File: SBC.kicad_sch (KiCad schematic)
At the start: 0 parts

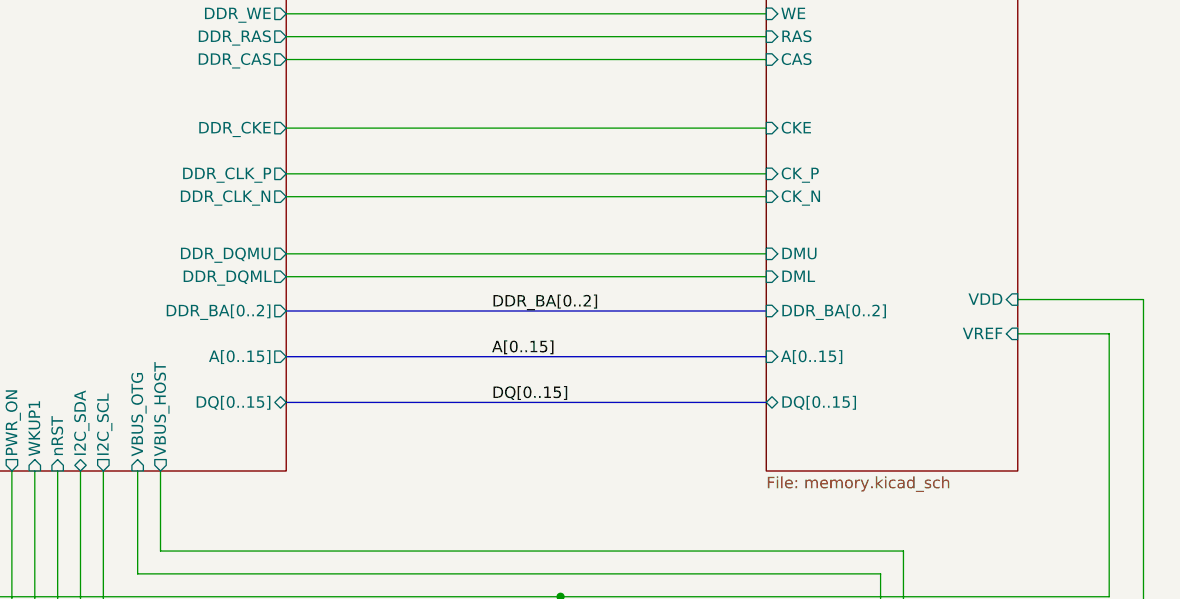
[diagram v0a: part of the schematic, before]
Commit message: DDR routing first pass complete
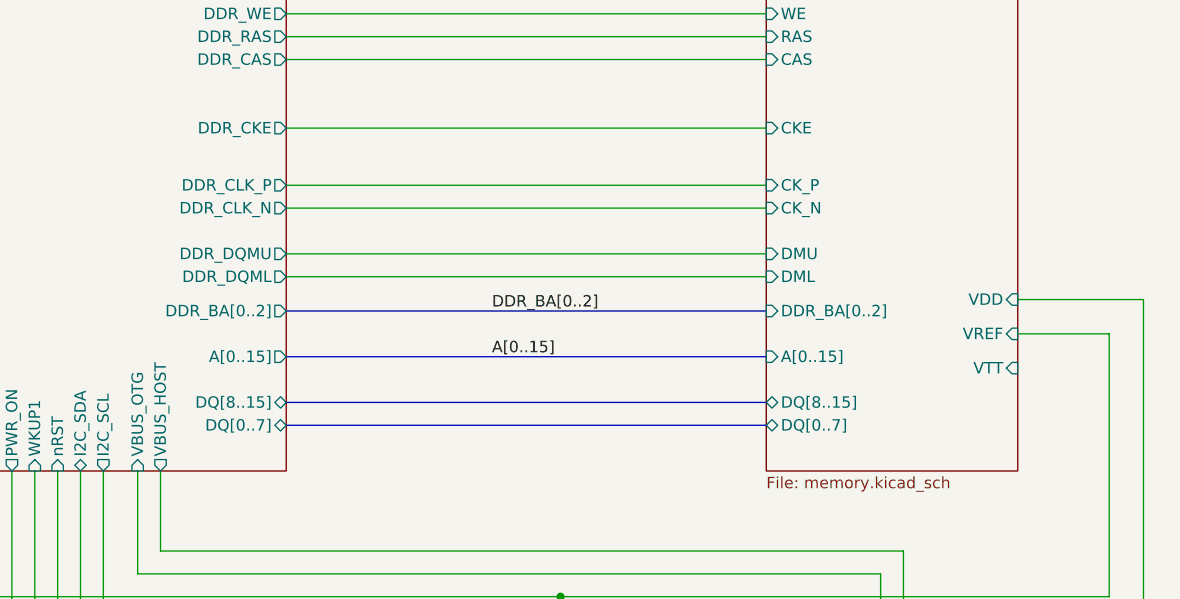
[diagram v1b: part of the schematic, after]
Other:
- sheet MPU ports: added DQ[0..7], DQ[8..15]; removed DQ[0..15]
- sheet Memory ports: added DQ[0..7], DQ[8..15], VTT; removed DQ[0..15]

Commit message: Routing routing routing
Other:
- sheet MPU ports: added SDMMC2_RESET, SDMMC2_STROBE; removed none
- sheet NAND ports: added DS; removed none
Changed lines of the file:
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@@
+	(wire
+		(pts
+			(xy 161.29 118.11) (xy 161.29 107.95)
+		)
+		(stroke
+			(width 0)
+			(type default)
+		)
+	)
 	(wire
 		(pts
@@
 	(wire
 		(pts
-			(xy 166.37 177.8) (xy 166.37 113.03)
+			(xy 168.91 177.8) (xy 168.91 115.57)
 		)
 		(stroke
@@
 	(wire
 		(pts
+			(xy 163.83 120.65) (xy 163.83 110.49)
+		)
+		(stroke
+			(width 0)
+			(type default)
+		)
+	)
+	(wire
+		(pts
 			(xy 205.74 142.24) (xy 205.74 205.74)
 		)
@@
 	(wire
 		(pts
+			(xy 161.29 107.95) (xy 179.07 107.95)
+		)
+		(stroke
+			(width 0)
+			(type default)
+		)
+	)
+	(wire
+		(pts
 			(xy 259.08 166.37) (xy 259.08 156.21)
 		)
@@
 	(wire
 		(pts
+			(xy 163.83 110.49) (xy 179.07 110.49)
+		)
+		(stroke
+			(width 0)
+			(type default)
+		)
+	)
+	(wire
+		(pts
 			(xy 214.63 142.24) (xy 214.63 151.13)
 		)
@@
 	(wire
 		(pts
+			(xy 147.32 118.11) (xy 161.29 118.11)
+		)
+		(stroke
+			(width 0)
+			(type default)
+		)
+	)
+	(wire
+		(pts
 			(xy 320.04 127) (xy 309.88 127)
 		)
@@
 	(wire
 		(pts
+			(xy 147.32 120.65) (xy 163.83 120.65)
+		)
+		(stroke
+			(width 0)
+			(type default)
+		)
+	)
+	(wire
+		(pts
 			(xy 228.6 74.93) (xy 281.94 74.93)
 		)
@@
 	(wire
 		(pts
-			(xy 166.37 113.03) (xy 179.07 113.03)
+			(xy 168.91 115.57) (xy 179.07 115.57)
 		)
 		(stroke
@@
 	(wire
 		(pts
-			(xy 234.95 177.8) (xy 166.37 177.8)
+			(xy 234.95 177.8) (xy 168.91 177.8)
 		)
 		(stroke
@@
 				(justify left bottom)
 				(hide yes)
+			)
+		)
+	)
+	(netclass_flag ""
+		(length 0.0254)
+		(shape round)
+		(at 154.94 100.33 0)
+		(effects
+			(font
+				(size 1.27 1.27)
+			)
+			(justify left bottom)
+		)
+		(property "Netclass" "EMMC"
+			(at 155.5496 100.3046 0)
+			(effects
+				(font
+					(size 1.27 1.27)
+					(italic yes)
+				)
+				(justify left bottom)
+			)
+		)
+	)
+	(netclass_flag ""
+		(length 0.0254)
+		(shape round)
+		(at 160.02 105.41 0)
+		(effects
+			(font
+				(size 1.27 1.27)
+			)
+			(justify left bottom)
+		)
+		(property "Netclass" "EMMC"
+			(at 160.6296 105.3846 0)
+			(effects
+				(font
+					(size 1.27 1.27)
+					(italic yes)
+				)
+				(justify left bottom)
 			)
 		)
@@
 		(length 0.0254)
 		(shape round)
+		(at 165.1 110.49 0)
+		(effects
+			(font
+				(size 1.27 1.27)
+			)
+			(justify left bottom)
+		)
+		(property "Netclass" "EMMC"
+			(at 165.7096 110.4646 0)
+			(effects
+				(font
+					(size 1.27 1.27)
+					(italic yes)
+				)
+				(justify left bottom)
+			)
+		)
+	)
+	(netclass_flag ""
+		(length 0.0254)
+		(shape round)
+		(at 157.48 102.87 0)
+		(effects
+			(font
+				(size 1.27 1.27)
+			)
+			(justify left bottom)
+		)
+		(property "Netclass" "EMMC"
+			(at 158.0896 102.8446 0)
+			(effects
+				(font
+					(size 1.27 1.27)
+					(italic yes)
+				)
+				(justify left bottom)
+			)
+		)
+	)
+	(netclass_flag ""
+		(length 0.0254)
+		(shape round)
 		(at 237.49 137.16 0)
 		(effects
@@
 		(property "Netclass" "DDR_DATA_L"
 			(at 234.2896 83.7946 0)
+			(effects
+				(font
+					(size 1.27 1.27)
+					(italic yes)
+				)
+				(justify left bottom)
+			)
+		)
+	)
+	(netclass_flag ""
+		(length 0.0254)
+		(shape round)
+		(at 162.56 107.95 0)
+		(effects
+			(font
+				(size 1.27 1.27)
+			)
+			(justify left bottom)
+		)
+		(property "Netclass" "EMMC"
+			(at 163.1696 107.9246 0)
 			(effects
 				(font
@@
 		)
 		(pin "VDDA" input
-			(at 179.07 113.03 180)
+			(at 179.07 115.57 180)
 			(effects
 				(font
@@
 				)
 				(justify right)
+			)
+		)
+		(pin "SDMMC2_STROBE" output
+			(at 179.07 107.95 180)
+			(effects
+				(font
+					(size 1.27 1.27)
+				)
+				(justify left)
+			)
+		)
+		(pin "SDMMC2_RESET" output
+			(at 179.07 110.49 180)
+			(effects
+				(font
+					(size 1.27 1.27)
+				)
+				(justify left)
 			)
 		)
@@
 		)
 		(pin "RESET" input
+			(at 147.32 120.65 0)
+			(effects
+				(font
+					(size 1.27 1.27)
+				)
+				(justify right)
+			)
+		)
+		(pin "DS" output
 			(at 147.32 118.11 0)
 			(effects

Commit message: More routing
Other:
- note added: "Notes"
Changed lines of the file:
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@@
+		)
+	)
+	(text_box "Trace width and spacing requirements:\n\n(Differential)\n1. 90 Ohm outer layer     -> W=0.1422mm, S=0.0994\n2. 100 Ohm outer layer    -> W=0.1095, S=0.0994\n3. 90 Ohm inner layer     -> W=0.1328, S=0.0994\n4. 100 Ohm innder layer   -> W=0.1029, S=0.0994\n\n(Single Ended)\n1. 45 Ohm outer layer     -> W=0.1542, T=0.0994\n2. 50 Ohm outer layer     -> W=0.1196, T=0.0994\n3. 55 Ohm outer layer     -> W=0.0922, T=0.0994\n4. 45 Ohm inner layer     -> W=0.1765, T=0.0994\n5. 50 Ohm inner layer     -> W=0.1425, T=0.0994\n6. 55 Ohm inner layer     -> W=0.1153, T=0.0994\n\nStack Up:\nLayer         Material                            Thickness (mm)\n\nL1            Outer Copper Weight 1.0oz           0.0350\nPrepreg       3313 RC57% 4.2mil                   0.0994\nL2            Inner Copper Weight 0.5oz           0.0152\nCore          0.55mm H/Hwithout copper            0.5500\nL3            Inner Copper Weight                 0.0152\nPrepreg       2116 RC54% 4.9mil                   0.1088\nL4            Inner Copper Weight                 0.0152\nCore          0.55mm H/Hwithout copper            0.5500\nL5            Inner Copper Weight                 0.0152\nPrepeg        3313 RC57% 4.2mil                   0.0994\nL6            Outer RC57% 4.2mil                  0.0350"
+		(exclude_from_sim no)
+		(at 334.01 19.05 0)
+		(size 81.28 64.77)
+		(stroke
+			(width 0)
+			(type default)
+			(color 255 255 0 1)
+		)
+		(fill
+			(type none)
+		)
+		(effects
+			(font
+				(face "Courier New")
+				(size 1.27 1.27)
+				(color 255 255 0 1)
+			)
+			(justify left top)
+		)
+	)
+	(text "Notes"
+		(exclude_from_sim no)
+		(at 337.058 18.796 0)
+		(effects
+			(font
+				(face "Courier New")
+				(size 1.27 1.27)
+				(color 255 255 0 1)
+			)
 		)
 	)
